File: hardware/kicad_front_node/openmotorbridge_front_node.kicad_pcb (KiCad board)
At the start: 2 copper layers, 68 x 44 mm, 37 parts, among them J1 OPT_12V_KL15_GND, J2 CAN_H_L_GND, J3 PTT_IN_GND, J4 USB_UPSTREAM_HOST, J5 USB_DN1_GLOVEBOX, J6 USB_DN2_CARPLAY, J7 USB-C_SERVICE, J8 J8: ACTION_CAM_5V_PWR, SW1 BOOT, SW2 RESET, U1 ESP32-C3-WROOM-02U, U2 USB2512B_AEC_HUB, U3 TPS2051B_CARPLAY_SWITCH, U4 TPS54302_BUCK_5V2A, U5 TCAN334G_CAN, U6 TLV75533P_3V3_500mA, Y1 24.000MHz

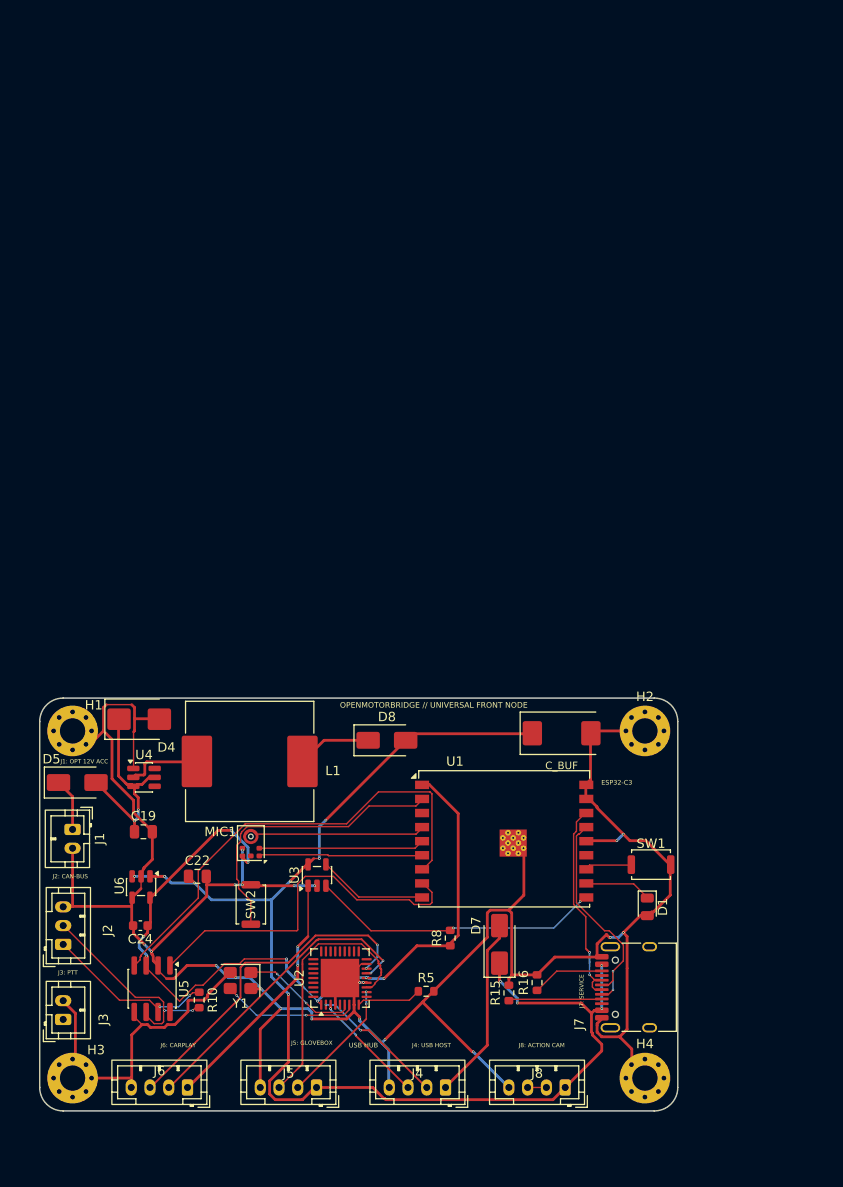
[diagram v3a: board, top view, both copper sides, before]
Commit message: feat(hw,fw,pwa): implement PCBA 05 Front Node, LoRa alarm pager, universal TPMS, ESS strobe, privacy mute, and video telemetry export
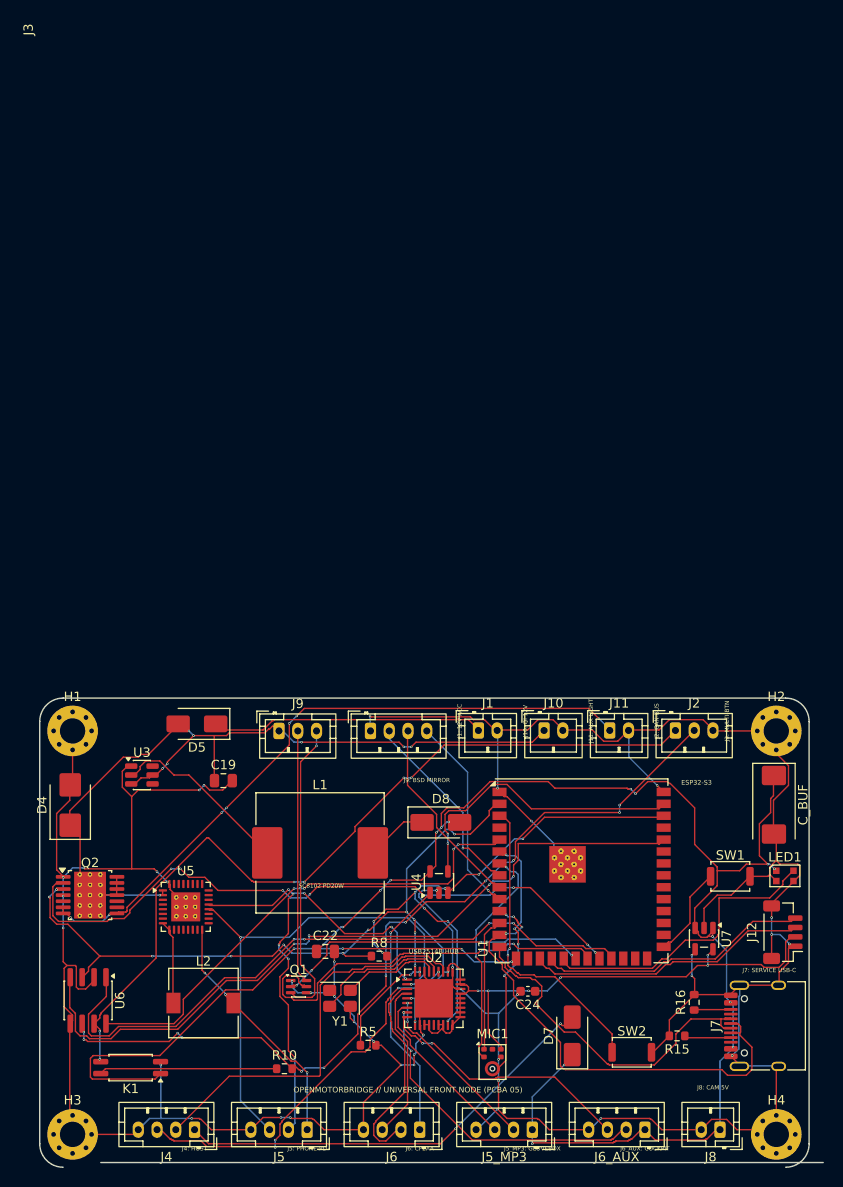
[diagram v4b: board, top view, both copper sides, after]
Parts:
- removed D1: LED_STATUS_GREEN, LED_0805_2012Metric
- added J10: 12V_QI_POWER, JST_PH_B2B-PH-K_1x02_P2.00mm_Vertical, F.Cu at (153.8, 73.5)
- added J11: 12V_AUX_LIGHT, JST_PH_B2B-PH-K_1x02_P2.00mm_Vertical, F.Cu at (160.8, 73.5)
- added J12: QWIIC_I2C, JST_SH_BM04B-SRSS-TB_1x04-1MP_P1.00mm_Vertical, F.Cu at (179.2, 95.0)
- added J5_MP3: USB_DN3_GLOVEBOX, JST_PH_B4B-PH-K_1x04_P2.00mm_Vertical, F.Cu at (152.5, 116.0)
- added J6_AUX: USB_DN4_COCKPIT_AUX, JST_PH_B4B-PH-K_1x04_P2.00mm_Vertical, F.Cu at (164.5, 116.0)
- added J9: MIRROR_BSD_LEDS, JST_PH_B3B-PH-K_1x03_P2.00mm_Vertical, F.Cu at (125.5, 73.5)
- added K1: CPC1017N_CAN_RELAY, SOP-4_4.4x2.6mm_P1.27mm, F.Cu at (109.7, 109.4)
- added L2: 10uH_PD_Choke, L_7.3x7.3_H4.5, F.Cu at (117.5, 102.5)
- added LED1: WS2812B-2020_RGB, LED_WS2812B-2020_PLCC4_2.0x2.0mm, F.Cu at (179.4, 89.0)
- added Q1: DMN63D8_BSD_MOSFET, SOT-363_SC-70-6, F.Cu at (127.6, 100.8)
- added Q2: TPS1H100_AUX_LIGHT, Texas_HTSSOP-14-1EP_4.4x5mm_P0.65mm_EP3.4x5mm_Mask3.155x3.255mm_ThermalVias, F.Cu at (105.4, 91.0)
- added U7: TLV75533P_3V3_LDO, SOT-23-5, F.Cu at (170.8, 95.6)
- J1: value OPT_12V_KL15_GND -> 12V_KL15_GND
- J3: value PTT_IN_GND -> HANDLEBAR_MULTI_BTN; footprint JST_PH_B2B-PH-K_1x02_P2.00mm_Vertical -> JST_PH_B4B-PH-K_1x04_P2.00mm_Vertical
- J5: value USB_DN1_GLOVEBOX -> USB_DN1_PHONE_PD20W
- J6: value USB_DN2_CARPLAY -> USB_DN2_CP2AA_PIGTAIL
- J8: value J8: ACTION_CAM_5V_PWR -> ACTION_CAM_5V_PWR; footprint JST_PH_B4B-PH-K_1x04_P2.00mm_Vertical -> JST_PH_B2B-PH-K_1x02_P2.00mm_Vertical
- U1: value ESP32-C3-WROOM-02U -> ESP32-S3-WROOM-1U; footprint ESP32-C3-WROOM-02U -> ESP32-S3-WROOM-1U
- U2: value USB2512B_AEC_HUB -> USB2514B_AEC_HUB
- U3: value TPS2051B_CARPLAY_SWITCH -> TPS54302_5V_BUCK; footprint SOT-23-5 -> SOT-23-6
- U4: value TPS54302_BUCK_5V2A -> TPS2051B_PORT2_GATE; footprint SOT-23-6 -> SOT-23-5
- U5: value TCAN334G_CAN -> SC8102_USB_PD_20W; footprint SOIC-8_3.9x4.9mm_P1.27mm -> QFN-32-1EP_5x5mm_P0.5mm_EP3.1x3.1mm_ThermalVias
- U6: value TLV75533P_3V3_500mA -> TCAN334G_CAN; footprint SOT-23-5 -> SOIC-8_3.9x4.9mm_P1.27mm
- moved J2 69.1 mm to (167.8, 73.5), turned to 0 degrees
- moved J3 44.9 mm to (135.2, 73.5), turned to 0 degrees
- moved J1 44.5 mm to (146.8, 73.5), turned to 0 degrees
- moved SW2 43.5 mm to (163.1, 107.8), turned to 0 degrees
- moved C24 41.9 mm to (152.0, 101.2)
- moved MIC1 34.7 mm to (148.2, 108.8), turned to 0 degrees
- moved U4 33.4 mm to (142.6, 89.6), turned to 90 degrees
- moved J4 27.1 mm to (116.5, 116.0)
- moved J6 25.2 mm to (140.5, 116.0)
- moved C_BUF 23.9 mm to (178.2, 81.4), turned to -90 degrees
- moved U3 21.5 mm to (110.9, 78.2), turned to 0 degrees
- moved R15 18.5 mm to (167.9, 106.0), turned to 180 degrees
- moved J8 17.1 mm to (172.5, 116.0)
- moved R16 16.9 mm to (169.8, 102.4)
- moved C22 15.8 mm to (130.4, 97.0)
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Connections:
- C19 pad 1: VIN_BUCK -> +12V_PROT
- D4 pad 1: VIN_BUCK -> +12V_PROT
- D5 pad 2: VIN_BUCK -> +12V_PROT
- J3 pad 1: PTT_RAW -> GND
- J3 pad 2: GND -> PTT_IN1_N
- J5 pad 1: VCC_5V -> VBUS_PD_OUT
- J7 pad SH: (no net) -> GND
- J8 pad 2: USB_CAM_DCP -> GND
- R10 pad 1: CAN_H -> CAN_TERM_R
- U1 pad 1: VCC_3V3 -> GND
- U1 pad 10: OTTOCAST_FAULT_N -> PTT_IN3_N
- U1 pad 11: LED_STATUS -> USB_SERV_DM
- U1 pad 12: ESP_BOOT -> MIC_I2S_DATA
- U1 pad 13: KL15_SENSE -> USB_SERV_DM
- U1 pad 14: GND -> USB_SERV_DP
- U1 pad 15: USB_SERV_DM -> CAN_TERM_EN
- U1 pad 16: USB_SERV_DP -> (no net)
- U1 pad 17: GND -> I2C_SDA
- U1 pad 18: GND -> I2C_SCL
- U1 pad 19: GND -> WS2812B_DIN
- U1 pad 2: ESP_EN -> VCC_3V3
- U1 pad 3: PTT_INPUT_N -> ESP_EN
- U1 pad 4: MIC_I2S_WS -> KL15_SENSE
- U1 pad 5: MIC_I2S_BCLK -> CAN_SILENT
- U1 pad 6: MIC_I2S_DATA -> MIC_I2S_WS
- U1 pad 7: TWAI_RX -> MIC_I2S_BCLK
- U1 pad 8: TWAI_TX -> PTT_IN1_N
- U1 pad 9: OTTOCAST_PWR_EN -> PTT_IN2_N
- U2 pad 1: VCC_3V3 -> USB_DN1_DM
- U2 pad 10: HUB_RESET_N -> VCC_3V3
- U2 pad 11: USB_DN1_DM -> GND
- U2 pad 12: USB_DN1_DP -> VCC_3V3
- U2 pad 13: GND -> VCC_3V3
- U2 pad 14: VCC_3V3 -> VDD12_HUB
- U2 pad 15: USB_DN2_DM -> VCC_3V3
- U2 pad 16: USB_DN2_DP -> VCC_3V3
- U2 pad 17: GND -> OTTOCAST_FAULT_N
- U2 pad 18: (no net) -> VCC_3V3
- U2 pad 19: (no net) -> VCC_3V3
- U2 pad 2: USB_UP_DM -> USB_DN1_DP
- U2 pad 20: (no net) -> VCC_3V3
- U2 pad 21: (no net) -> VCC_3V3
- U2 pad 22: (no net) -> VCC_3V3
- U2 pad 23: (no net) -> VCC_3V3
- U2 pad 24: (no net) -> VCC_3V3
- U2 pad 25: (no net) -> GND
- U2 pad 26: (no net) -> VCC_3V3
- U2 pad 27: (no net) -> VCC_3V3
- U2 pad 28: (no net) -> GND
- U2 pad 29: (no net) -> VCC_3V3
- U2 pad 3: USB_UP_DP -> USB_DN2_DM
- U2 pad 30: (no net) -> USB_UP_DM
- U2 pad 31: (no net) -> USB_UP_DP
- U2 pad 32: (no net) -> XTAL_OUT
- U2 pad 33: (no net) -> XTAL_IN
- U2 pad 34: (no net) -> GND
- U2 pad 35: (no net) -> HUB_RBIAS
- U2 pad 36: (no net) -> VCC_3V3
- U2 pad 4: GND -> USB_DN2_DP
- U2 pad 5: VDD12_HUB -> VCC_3V3
- U2 pad 6: XTAL_IN -> USB_DN3_DM
- U2 pad 7: XTAL_OUT -> USB_DN3_DP
- U2 pad 8: GND -> USB_DN4_DM
- U2 pad 9: HUB_RBIAS -> USB_DN4_DP
- U3 pad 1: VCC_5V_OTTOCAST -> GND
- U3 pad 2: GND -> SW_BUCK
- U3 pad 3: OTTOCAST_FAULT_N -> +12V_PROT
- U3 pad 4: OTTOCAST_PWR_EN -> FB_BUCK
- U3 pad 5: VCC_5V -> +12V_PROT
- U4 pad 1: GND -> VCC_5V_OTTOCAST
- U4 pad 2: SW_BUCK -> GND
- U4 pad 3: VIN_BUCK -> OTTOCAST_FAULT_N
- U4 pad 4: FB_BUCK -> OTTOCAST_PWR_EN
- U4 pad 5: VIN_BUCK -> VCC_5V
- U5 pad 1: TWAI_TX -> +12V_PROT
- U5 pad 2: GND -> +12V_PROT
- U5 pad 3: VCC_3V3 -> (no net)
- U5 pad 4: TWAI_RX -> (no net)
- U5 pad 5: GND -> (no net)
- U5 pad 6: CAN_L -> (no net)
- U5 pad 7: CAN_H -> (no net)
- U5 pad 8: (no net) -> SW_PD_BUCK
- U6 pad 1: VCC_5V -> TWAI_TX
- U6 pad 3: VCC_5V -> VCC_3V3
- U6 pad 4: GND -> TWAI_RX
- U6 pad 5: VCC_3V3 -> GND
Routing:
- net GND: track 299.5 -> 395.9 mm, vias 21 -> 40
- net +12V_PROT: track 0.00 -> 88.8 mm, vias 0 -> 8
- net +12V_AUX: track 0.00 -> 71.4 mm, vias 0 -> 7
- net VCC_3V3: track 86.6 -> 157.9 mm, vias 8 -> 21
- net AUX_LIGHT_EN: track 0.00 -> 70.3 mm, vias 0 -> 8
- net CAN_H: track 18.5 -> 88.2 mm, vias 2 -> 6
- net CAN_L: track 22.9 -> 90.6 mm, vias 2 -> 12
- net CAN_TERM_EN: track 0.00 -> 60.9 mm, vias 0 -> 4
- net CAN_SILENT: track 0.00 -> 52.8 mm, vias 0 -> 4
- net USB_DN1_DM: track 13.2 -> 56.4 mm, vias 2 -> 8
- net BSD_LED_RIGHT: track 0.00 -> 42.3 mm, vias 0 -> 2
- net BSD_LED_LEFT: track 0.00 -> 34.0 mm, vias 0 -> 4
- net USB_DN4_DM: track 0.00 -> 33.7 mm, vias 0 -> 2
- net BSD_RIGHT_N: track 0.00 -> 32.3 mm, vias 0 -> 1
- net WS2812B_DIN: track 0.00 -> 32.0 mm
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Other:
- board size 68 x 44 mm -> 83.5 x 50 mm
- board text added: "ESP32-S3"
- board text added: "J10: QI 12V"
- board text added: "J11: AUX LIGHT"
- board text added: "J1: 12V ACC"
- board text added: "J3: MULTI-BTN"
- board text added: "J4: HOST"
- board text added: "J5: PHONE-PD"
- board text added: "J5_MP3: GLOVEBOX"
- board text added: "J6: CP2AA"
- board text added: "J6_AUX: COCKPIT"
- board text added: "J7: SERVICE USB-C"
- board text added: "J8: CAM 5V"
- board text added: "J9: BSD MIRROR"
- board text added: "OPENMOTORBRIDGE // UNIVERSAL FRONT NODE (PCBA 05)"
- board text added: "SC8102 PD20W"
- board text added: "USB2514B HUB"
- board text removed: "ESP32-C3"
- board text removed: "J1: OPT 12V ACC"
- board text removed: "J3: PTT"
- board text removed: "J4: USB HOST"
- board text removed: "J5: GLOVEBOX"
- board text removed: "J6: CARPLAY"
- board text removed: "J7: SERVICE"
- board text removed: "J8: ACTION CAM"
- board text removed: "OPENMOTORBRIDGE // UNIVERSAL FRONT NODE"
- board text removed: "USB HUB"

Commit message: feat(hardware): implement dual independent 20W USB-PD subsystem for Lenker and Handschuhfach on PCBA 05
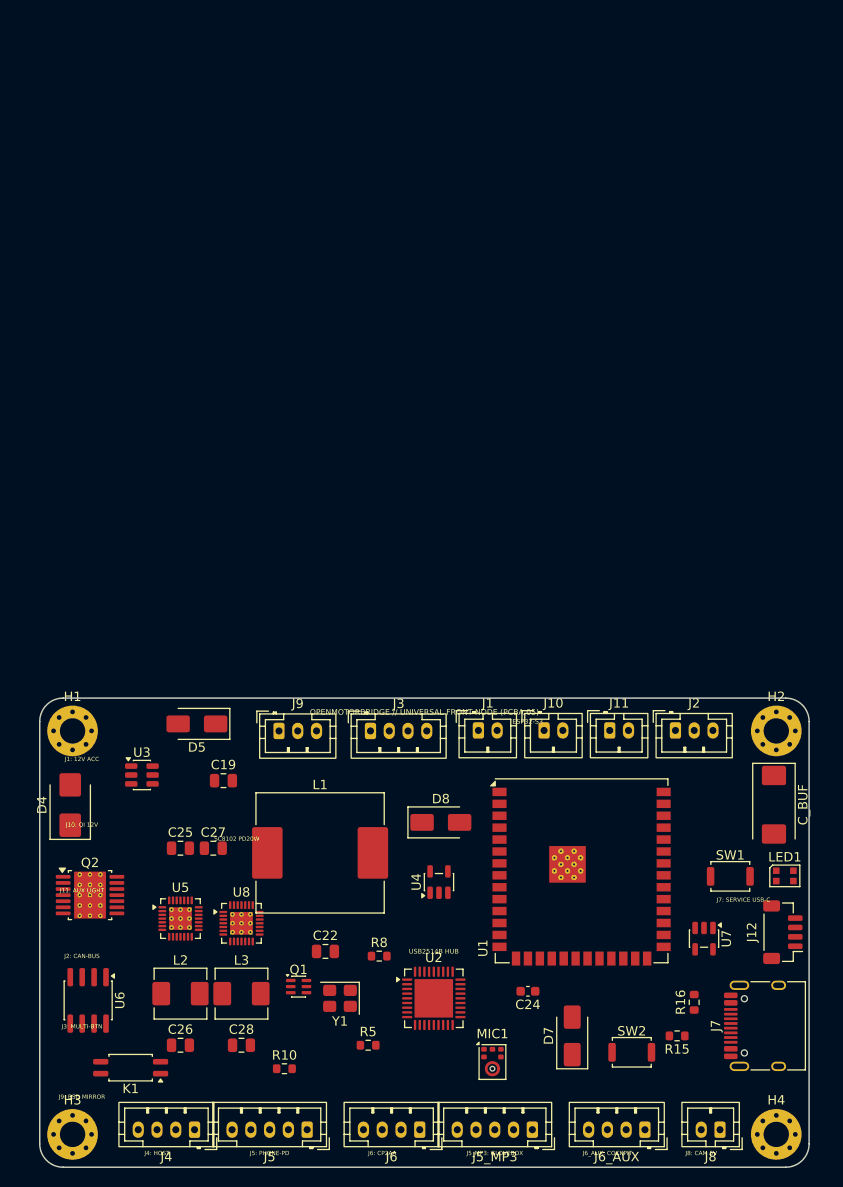
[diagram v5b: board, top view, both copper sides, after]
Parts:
- added C25: 10uF_50V_PD1, C_0805_2012Metric, F.Cu at (115.0, 86.0)
- added C26: 22uF_25V_PD1, C_0805_2012Metric, F.Cu at (115.0, 107.0)
- added C27: 10uF_50V_PD3, C_0805_2012Metric, F.Cu at (118.5, 86.0)
- added C28: 22uF_25V_PD3, C_0805_2012Metric, F.Cu at (121.5, 107.0)
- added L3: 4.7uH_PD3_Choke, L_Sunlord_MWSA0503S, F.Cu at (121.5, 101.5)
- added U8: SW3526_USB_PD3_20W, QFN-28-1EP_4x4mm_P0.4mm_EP2.4x2.4mm_ThermalVias, F.Cu at (121.5, 94.0)
- J5: footprint JST_PH_B4B-PH-K_1x04_P2.00mm_Vertical -> JST_PH_B5B-PH-K_1x05_P2.00mm_Vertical
- J5_MP3: value USB_DN3_GLOVEBOX -> USB_DN3_GLOVEBOX_PD20W; footprint JST_PH_B4B-PH-K_1x04_P2.00mm_Vertical -> JST_PH_B5B-PH-K_1x05_P2.00mm_Vertical
- L2: value 10uH_PD_Choke -> 4.7uH_PD1_Choke; footprint L_7.3x7.3_H4.5 -> L_Sunlord_MWSA0503S
- U5: value SC8102_USB_PD_20W -> SW3526_USB_PD1_20W; footprint QFN-32-1EP_5x5mm_P0.5mm_EP3.1x3.1mm_ThermalVias -> QFN-28-1EP_4x4mm_P0.4mm_EP2.4x2.4mm_ThermalVias
- moved L2 2.65 mm to (115.0, 101.5)
- moved U5 1.37 mm to (115.0, 93.5)
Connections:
- J5 pad 1: VBUS_PD_OUT -> VBUS_PD1_OUT
- J5 pad 4: GND -> USB_DN1_CC
- J5_MP3 pad 1: VCC_5V -> VBUS_PD3_OUT
- J5_MP3 pad 4: GND -> USB_DN3_CC
- L2 pad 1: SW_PD_BUCK -> SW_PD1_BUCK
- L2 pad 2: VBUS_PD_OUT -> VBUS_PD1_OUT
- U5 pad 14: (no net) -> GND
- U5 pad 16: VBUS_PD_OUT -> USB_DN1_DP
- U5 pad 17: (no net) -> USB_DN1_DM
- U5 pad 18: (no net) -> USB_DN1_CC
- U5 pad 19: (no net) -> USB_DN1_CC
- U5 pad 20: USB_DN1_DP -> (no net)
- U5 pad 21: USB_DN1_DM -> VBUS_PD1_OUT
- U5 pad 25: (no net) -> SW_PD1_BUCK
- U5 pad 26: (no net) -> SW_PD1_BUCK
- U5 pad 27: (no net) -> SW_PD1_BUCK
- U5 pad 28: (no net) -> +12V_PROT
- U5 pad 29: (no net) -> GND
- U5 pad 8: SW_PD_BUCK -> (no net)
- U5 pad 9: SW_PD_BUCK -> (no net)
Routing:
- net GND: track 395.9 -> 0.00 mm, vias 40 -> 0
- net VCC_3V3: track 157.9 -> 0.00 mm, vias 21 -> 0
- net VCC_5V: track 146.9 -> 0.00 mm, vias 16 -> 0
- net CAN_L: track 90.6 -> 0.00 mm, vias 12 -> 0
- net +12V_PROT: track 88.8 -> 0.00 mm, vias 8 -> 0
- net CAN_H: track 88.2 -> 0.00 mm, vias 6 -> 0
- net TWAI_RX: track 80.1 -> 0.00 mm, vias 4 -> 0
- net +12V_AUX: track 71.4 -> 0.00 mm, vias 7 -> 0
- net AUX_LIGHT_EN: track 70.3 -> 0.00 mm, vias 8 -> 0
- net TWAI_TX: track 69.4 -> 0.00 mm, vias 4 -> 0
- net CAN_TERM_EN: track 60.9 -> 0.00 mm, vias 4 -> 0
- net OTTOCAST_FAULT_N: track 57.9 -> 0.00 mm, vias 9 -> 0
- net USB_DN1_DM: track 56.4 -> 0.00 mm, vias 8 -> 0
- net USB_DN1_DP: track 54.1 -> 0.00 mm, vias 2 -> 0
- net CAN_SILENT: track 52.8 -> 0.00 mm, vias 4 -> 0
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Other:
- board size 83.5 x 50 mm -> 82 x 50 mm
- net class Default added: clearance 0.127, trace_width 0.15, via_dia 0.6, via_drill 0.3
- net class Power added: clearance 0.15, trace_width 0.3, via_dia 0.6, via_drill 0.3
- net class USB_DIFF added: clearance 0.15, trace_width 0.2, via_dia 0.6, via_drill 0.3

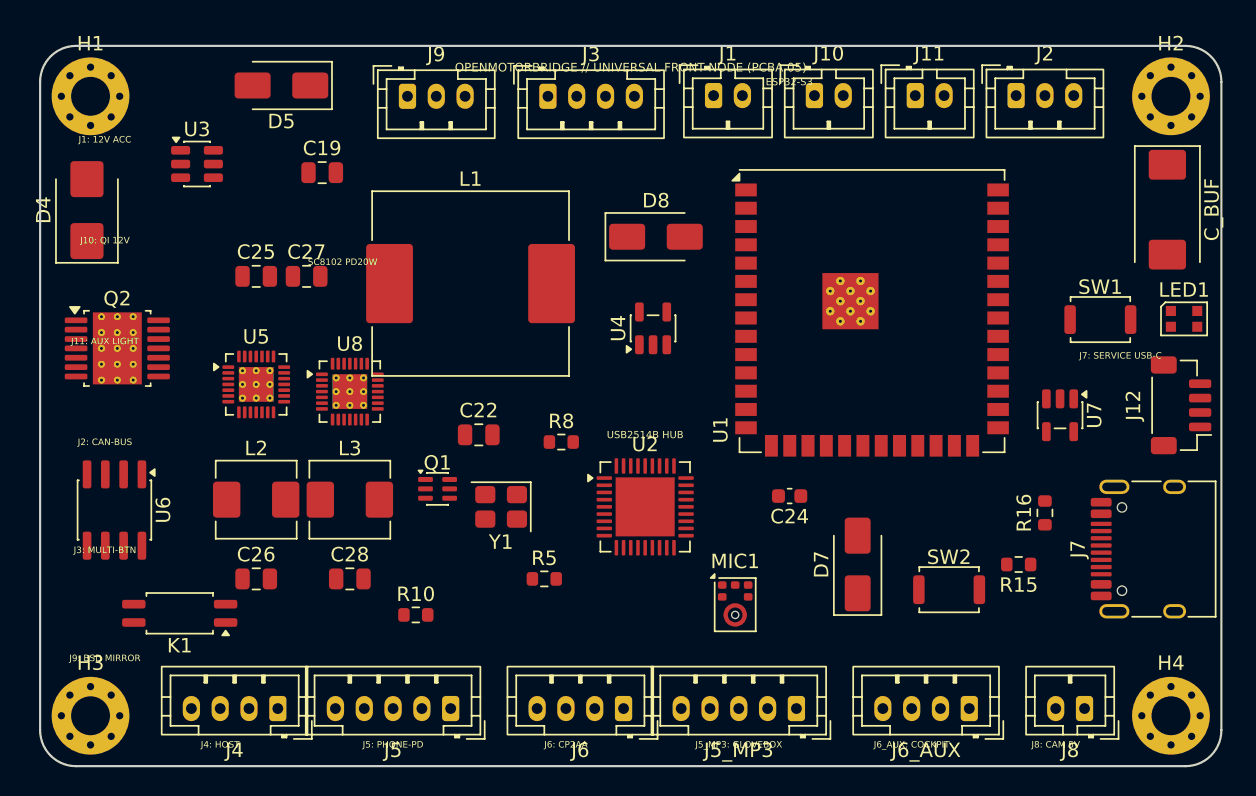
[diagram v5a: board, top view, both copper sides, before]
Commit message: hardware(front-node): complete dual 20W USB-PD routing and sync manufacturing packages
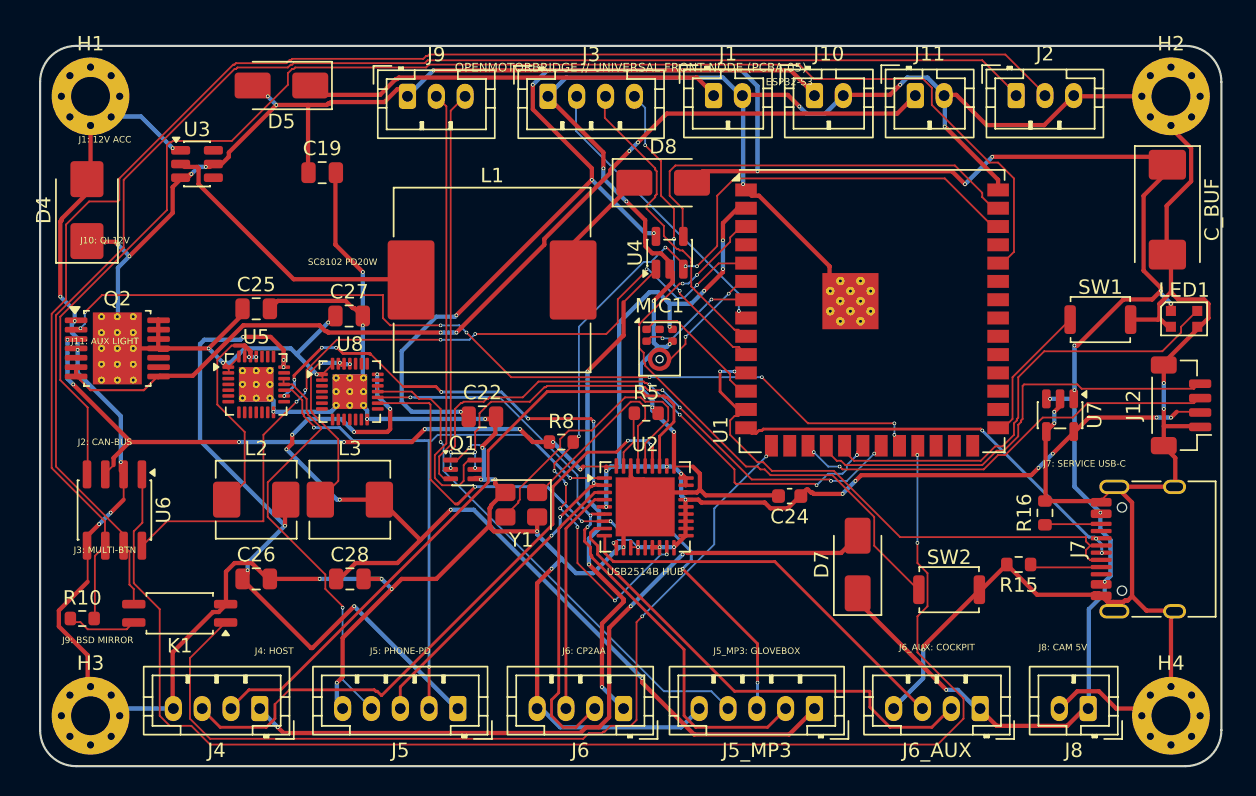
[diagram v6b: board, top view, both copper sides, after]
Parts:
- moved R10 23.2 mm to (102.9, 109.8)
- moved MIC1 18.5 mm to (143.0, 91.0)
- moved R5 13.5 mm to (142.1, 95.5)
- moved U4 5.37 mm to (143.7, 84.4)
- moved C27 4.03 mm to (121.5, 88.8)
- moved D8 3.78 mm to (143.2, 79.5)
- moved C25 2.25 mm to (115.0, 88.2)
- moved Q1 2.21 mm to (129.3, 99.4)
- moved L1 1.52 mm to (131.4, 86.2)
- moved Y1 1.41 mm to (133.4, 101.8)
- moved C22 1.27 mm to (130.7, 95.8)
- moved J4 1.25 mm to (115.2, 116.0)
- moved J5_MP3 1.25 mm to (153.8, 116.0)
- moved J6_AUX 0.75 mm to (165.2, 116.0)
- moved J5 0.50 mm to (129.0, 116.0)
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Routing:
- net GND: track 0.00 -> 412.8 mm, vias 0 -> 38
- net VCC_5V: track 0.00 -> 168.4 mm, vias 0 -> 16
- net VCC_3V3: track 0.00 -> 135.3 mm, vias 0 -> 27
- net CAN_L: track 0.00 -> 104.7 mm
- net CAN_H: track 0.00 -> 100.2 mm
- net +12V_PROT: track 0.00 -> 99.6 mm, vias 0 -> 11
- net TWAI_RX: track 0.00 -> 98.8 mm
- net TWAI_TX: track 0.00 -> 96.1 mm, vias 0 -> 2
- net +12V_AUX: track 0.00 -> 68.8 mm, vias 0 -> 4
- net VBUS_PD3_OUT: track 0.00 -> 67.6 mm, vias 0 -> 8
- net OTTOCAST_FAULT_N: track 0.00 -> 65.5 mm, vias 0 -> 10
- net AUX_LIGHT_EN: track 0.00 -> 64.7 mm, vias 0 -> 8
- net CAN_TERM_EN: track 0.00 -> 62.8 mm, vias 0 -> 2
- net CAN_SILENT: track 0.00 -> 57.1 mm, vias 0 -> 6
- net USB_DN1_DP: track 0.00 -> 52.4 mm, vias 0 -> 10
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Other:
- net class Default removed
- net class Power removed
- net class USB_DIFF removed

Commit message: feat(hardware): add captive M3 nut pockets to main box and update PCBA05 MEMS/USB BOM
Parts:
- MIC1: value SPH0645_I2S_MIC -> MSM261S4030H0R; footprint Knowles_SPH0645LM4H-6_3.5x2.65mm -> InvenSense_ICS-43434-6_3.5x2.65mm
- U2: value USB2514B_AEC_HUB -> USB2514Bi-AEZG
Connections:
- MIC1 pad 1: MIC_I2S_DATA -> MIC_I2S_WS
- MIC1 pad 2: MIC_I2S_BCLK -> GND
- MIC1 pad 3: MIC_I2S_WS -> GND
- MIC1 pad 4: GND -> MIC_I2S_BCLK
- MIC1 pad 6: (no net) -> MIC_I2S_DATA
